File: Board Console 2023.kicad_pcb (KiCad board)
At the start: 6 copper layers, 214.2 x 98 mm, 201 parts, among them J1 Raspberry PI, J10 I2C_Conn, J11 USB_C, J13 SpeakerL, J14 SpeakerR, J15 Rasp_HDMI, J16 HDMI_OUT, J17 TTL 40Pin, J18 I2C EDID, J2 Composite OUT, J3 L1/L2, J4 SJ1-3525N, J5 USB_B_Micro, J6 Display, J7 USB_A, J8 R1/R2, J9 V_BATT, SW10 A, SW11 X, SW12 Down, SW13 Left, SW14 Up, SW15 Right, SW16 PWR_Push, SW17 SuperDX, SW3 Vol -, SW4 SuperSX, SW5 Select, SW6 Vol +, SW7 Start, SW8 B, SW9 Y, U1 MP3438GTL-P, U10 TS3DV642A0RUAR, U11 LM1117DT-3.3, U12 FAN5333BSX, U13 TFP401APZPR, U14 24LC02BT-E/LT, U15 LTC2950CTS8-1-TRMPBF, U2 MP3421GG-Z, U3 LM1117DT-3.3, U4 MP2722GRH-0000-P, U5 ADS1115IDGS, U6 NC7WV16P6X, U7 PAM8302AAD, U8 PAM8302AAD, U9 LM1117DT-3.3

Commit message: update layout pcb & zip tesi
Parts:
- added D6: BAV99, Package_TO_SOT_SMD:SOT-23, F.Cu at (247.1, 101.3)
- added G***: LOGO, Libs:nurburg, B.Cu at (61.9, 122.2)
- added JP7: SJ, Jumper:SolderJumper-2_P1.3mm_Open_Pad1.0x1.5mm, F.Cu at (148.5, 129.7)
- C50, C51: value C -> 0.033uF
- C52: value 0,033uF -> 0.01uF
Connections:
- J4 pad 1: GND -> Net-(D6-K-Pad3)
- J7 pad 5: GND -> Net-(J7-Shield)
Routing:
- net GND: track 266.2 -> 249.0 mm, vias 152 -> 153
- net Net-(J7-Shield): track 0.00 -> 16.0 mm
- net Net-(D6-K-Pad3): track 0.00 -> 8.01 mm
- net +5V: track 93.3 -> 94.4 mm, vias 21 -> 22
- net /Power Stage/EN: track 151.6 -> 152.5 mm
- net +3.3V: track 211.1 -> 210.5 mm
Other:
- board text added: "The Dollander Rev.1"

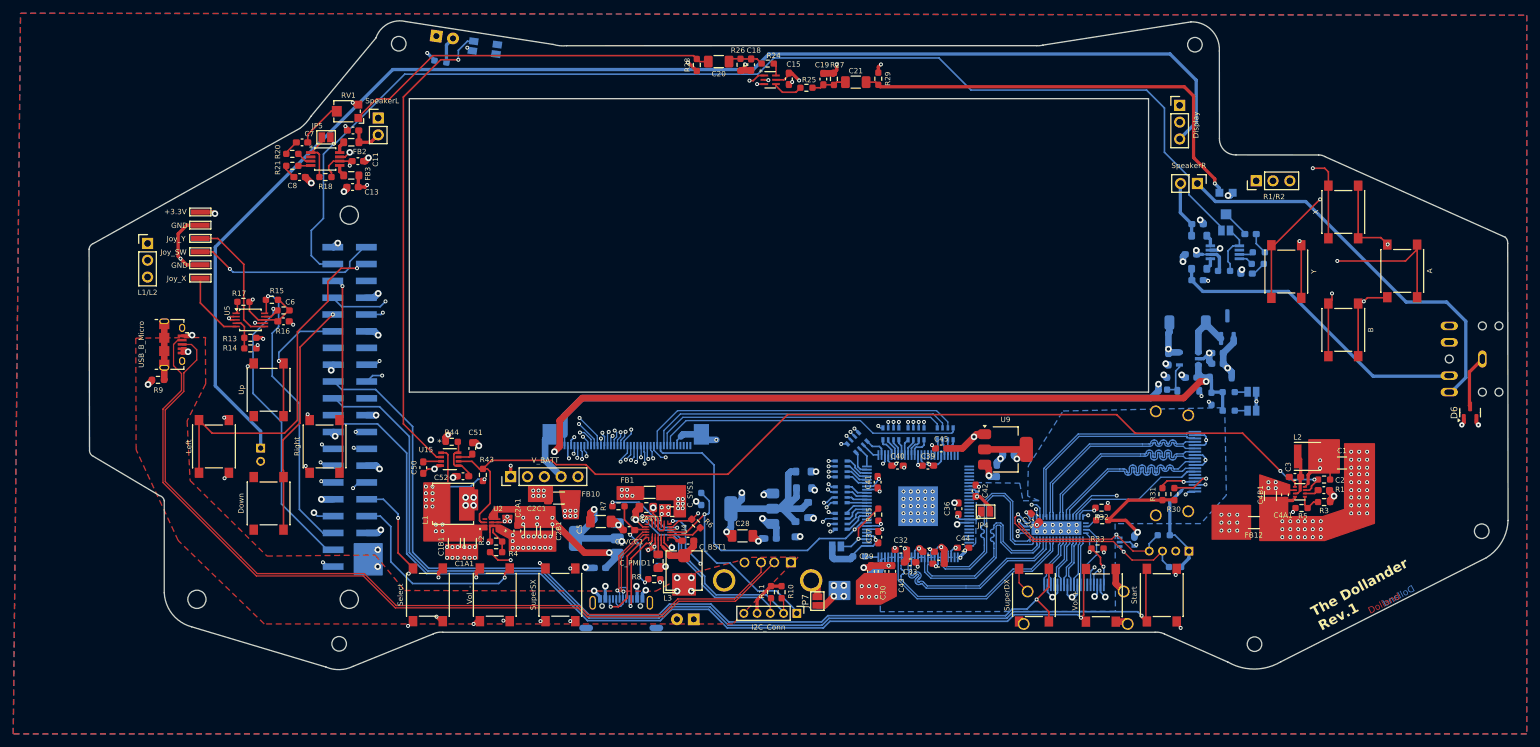
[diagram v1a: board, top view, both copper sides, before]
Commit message: edit posizioni porte e di alcune piste
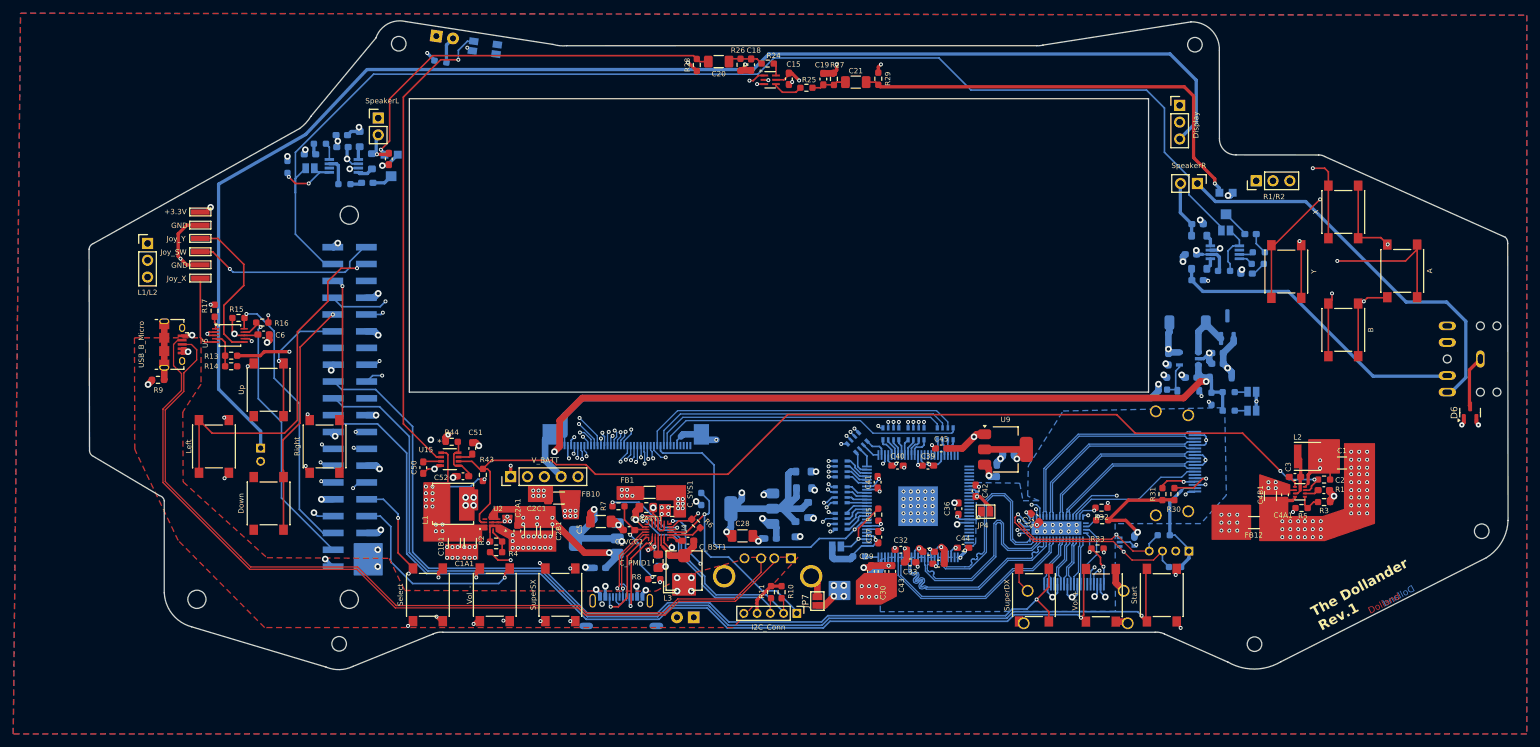
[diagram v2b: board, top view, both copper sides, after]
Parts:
- C11, C13, C7, C8, FB2, FB3, JP5, R18, R20, R21, RV1, U7: moved to B.Cu
- moved C7 11.6 mm to (80.5, 66.6)
- moved RV1 10.7 mm to (84.2, 64.2), turned to -90 degrees
- moved R20 9.10 mm to (77.1, 66.8), turned to 180 degrees
- moved C13 8.00 mm to (76.7, 59.4)
- moved C16 6.90 mm to (83.8, 63.0), turned to -90 degrees
- moved R18 5.93 mm to (68.5, 64.2), turned to -90 degrees
- moved R15 5.74 mm to (61.1, 87.0), turned to 0 degrees
- moved FB3 5.63 mm to (79.4, 60.0), turned to 90 degrees
- moved R21 5.34 mm to (73.4, 60.7)
- moved JP5 5.26 mm to (71.9, 64.4), turned to 0 degrees
- moved R17 4.55 mm to (57.5, 85.9), turned to -90 degrees
- moved FB2 4.23 mm to (81.2, 63.4), turned to 90 degrees
- moved R13 3.96 mm to (60.0, 92.7)
- moved R14 3.96 mm to (60.0, 94.3)
- moved U5 3.87 mm to (59.8, 89.6)
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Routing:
- net /Composite OUT: track 204.9 -> 180.1 mm
- net RASP_3.3V: track 95.0 -> 84.0 mm, vias 3 -> 5
- net Net-(C13-Pad1): track 218.0 -> 208.9 mm
- net /HDMI Switch/CK+: track 30.9 -> 23.5 mm
- net SHTDWN: track 179.2 -> 186.5 mm, vias 1 -> 0
- net /HDMI Switch/CK-: track 30.0 -> 23.0 mm
- net /HDMI Switch/D0+: track 31.2 -> 26.4 mm
- net /HDMI Switch/D0-: track 30.7 -> 25.9 mm
- net SDA: track 46.2 -> 42.1 mm
- net Net-(C7-Pad1): track 7.03 -> 3.15 mm
- net Joy_Y: track 20.1 -> 23.5 mm
- net /Audio Filter & Amplifier/OUT_L: track 57.2 -> 60.4 mm, vias 0 -> 1
- net Net-(JP5-B): track 7.87 -> 10.4 mm, vias 0 -> 2
- net +5V: track 94.4 -> 91.8 mm, vias 22 -> 23
- net GND: track 249.0 -> 251.3 mm, vias 153 -> 150
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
